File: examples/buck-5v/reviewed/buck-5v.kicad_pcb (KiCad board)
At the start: 2 copper layers, 126 x 56 mm, 11 parts, among them J1 12V IN, J2 5V OUT, U1 LM2596S-5

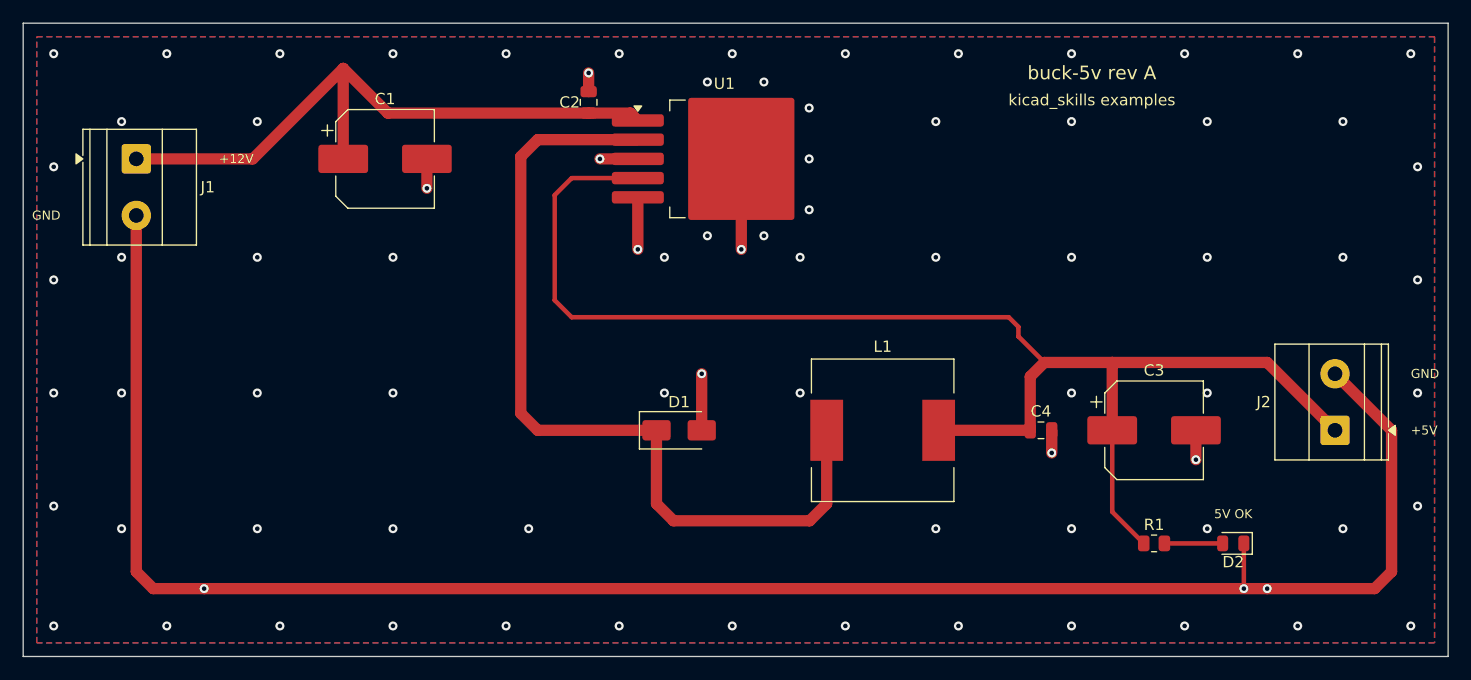
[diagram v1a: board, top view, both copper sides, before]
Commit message: Relieve the pads, fillet the joints, and give the board its screw holes
Three of the reviewer's manufacturing points, and they largely fall out
of the one before it - once KiCad fills the plane, the thermal relief it
was already asked for in the file actually appears.

**Thermal relief.** The zones said thermal all along; our own filler
ignored it and flooded every land solid. KiCad's does not, so every
through-hole ground pad now sits in a gap bridged by four spokes and an
iron can bring the joint up without heating a hundred square millimetres
of copper. `layout.solid_pad_connection` reports the setting when a
board turns it off: drilled pads only, because a surface pad reflows in
an oven that is heating the plane anyway and flooding it is often the
better thermal answer.

**Teardrops.** A track entering a land is a step change in width, and a
step change is where copper tears - the connector gets levered on and
off, the drill wanders, and the crack starts at the corner. `_teardrops`
replaces the first stretch of each run with a three-step taper into the
land, checked against its neighbours before it is kept, so a fillet
never eats the clearance a fine-pitch escape needs. It *replaces* rather
than overlays: laying the taper on top of the run drew the same copper
twice, and `route.acute_angle` reported all thirty of them, correctly.
`route.mixed_track_widths` learns what a fillet looks like so a properly
filleted board does not read as one nobody decided the width of.

**Mounting holes.** Four M3 holes near the corners, placed before the
router runs because they are obstacles, and slid along the edges or a
little inboard where a connector body has the corner - the motor board
and the op-amp take three, which is what those floorplans have room for.
Grounded on the motor driver, whose chassis is metal and part of the
shield, plain on the rest: bonding the enclosure to the reference is the
enclosure's decision, not the board's.

Two things that fell out of placing par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
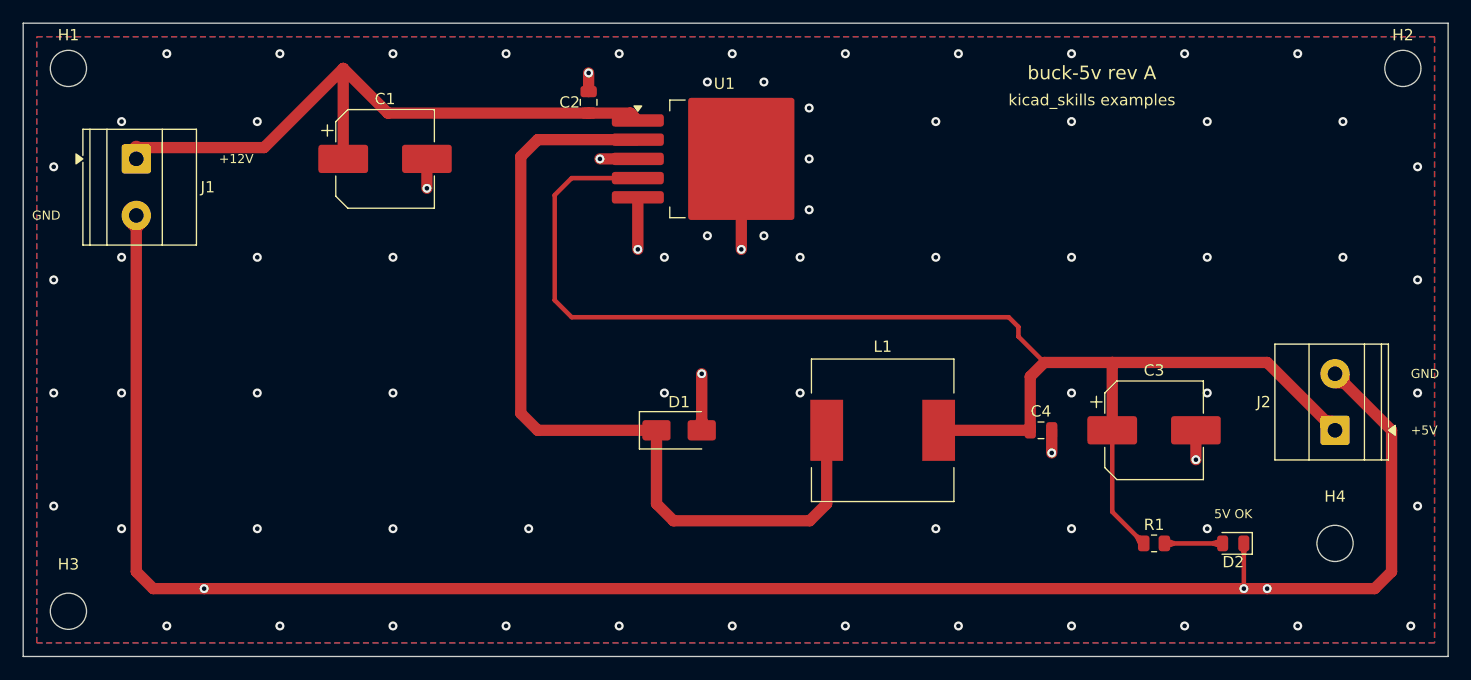
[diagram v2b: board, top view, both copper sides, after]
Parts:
- added H1: M33, MountingHole:MountingHole_3.2mm_M3, F.Cu at (104.0, 64.0)
- added H2: M33, MountingHole:MountingHole_3.2mm_M3, F.Cu at (222.0, 64.0)
- added H3: M33, MountingHole:MountingHole_3.2mm_M3, F.Cu at (104.0, 112.0)
- added H4: M33, MountingHole:MountingHole_3.2mm_M3, F.Cu at (216.0, 106.0)
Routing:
- net /+12V: track 57.6 -> 58.2 mm
- net GND: vias 82 -> 78

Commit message: Give the assembly machine something to aim at
Fiducials: three copper dots in bare mask windows, near three different
corners so a pick-and-place gets rotation as well as offset. It aligns
to the board, not to the drawing - without them it has only the routed
outline, cut to a tolerance ten times looser than the placement a 0.5 mm
pitch part is asking for. `fab.no_fiducials` reports a fine-pitch board
that has none, as context rather than as a fault: plenty of boards are
built one at a time with tweezers.

They share the corner search with the mounting holes, which is where
this found a real bug: `_courtyard_box` read lines and rectangles only,
and a mounting hole draws its courtyard as one circle - so every hole
measured as taking up no room at all, and the first three fiducials
landed on top of three screw holes. Circles and arcs count now.

Co-Authored-By: Claude Fable 5 <noreply@anthropic.com>
Claude-Session: https://claude.ai/code/session_01DUj7Ltu92tWg159mCSacwY
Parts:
- added FID1: Fiducial, Fiducial:Fiducial_1mm_Mask2mm, F.Cu at (102.5, 69.5)
- added FID2: Fiducial, Fiducial:Fiducial_1mm_Mask2mm, F.Cu at (216.5, 62.5)
- added FID3: Fiducial, Fiducial:Fiducial_1mm_Mask2mm, F.Cu at (109.5, 113.5)
- H1, H2, H3, H4: value M33 -> M3

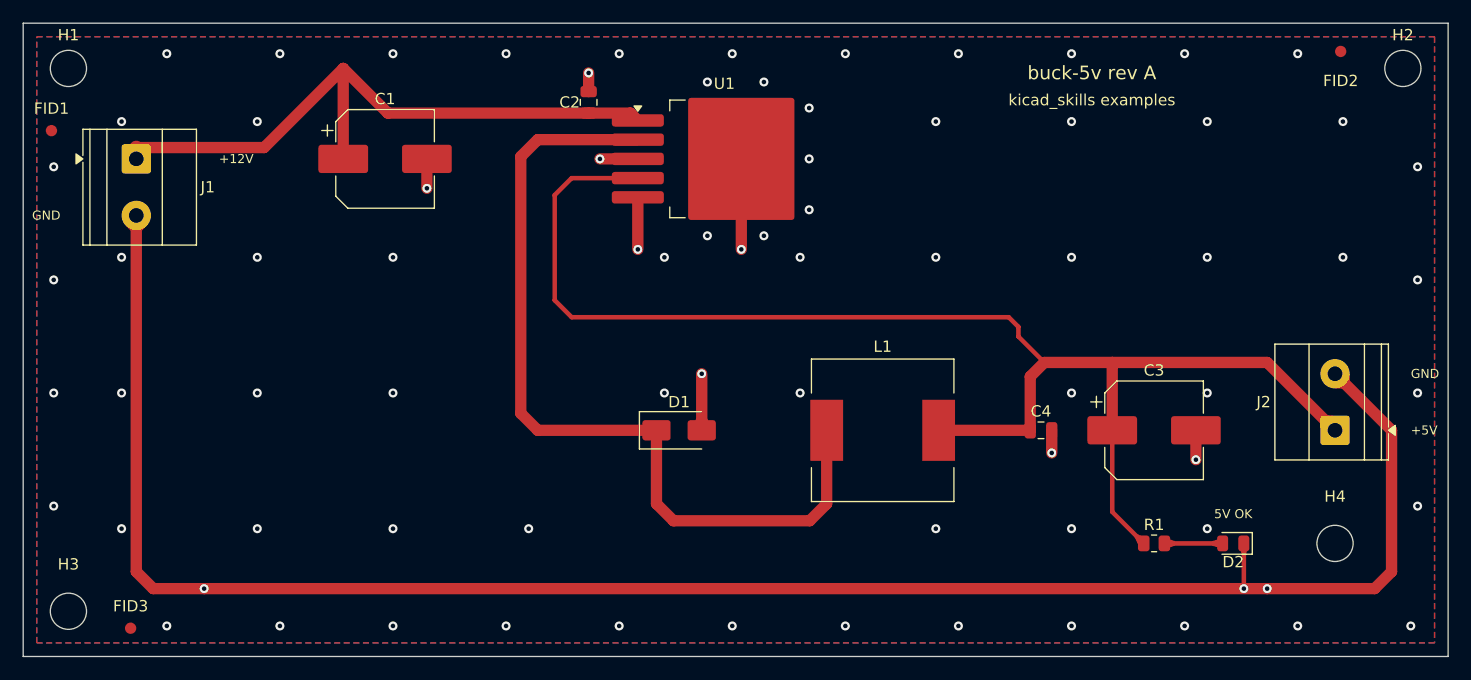
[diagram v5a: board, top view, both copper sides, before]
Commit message: Leave room for the screw, and print the ink where the board is
The screw holes were placed against the hole's own courtyard, which is the
drill plus a whisker - so on four of the five boards a hole sat inside a
connector's mating space, closest 0.42 mm. What goes through an M3 hole is a
pan head on a washer, seven millimetres of steel lying flat, and a connector
wants its shell, its wires and the fingers that fit them on top of that. The
spot search now keeps the fastener's own circle clear of every part body and
gives connectors CONNECTOR_ACCESS more, and three rules say so when a board
does not: mechanical.fastener_clearance, mechanical.connector_access and
mechanical.fastener_copper, all blocking for a generated design.

Silk was measured with a per-character advance of 0.78, and KiCad's stroke
font is proportional at 0.94 to 1.07. Everything downstream of that estimate
was placing ink where it did not fit: a legend across a capacitor's land, a
designator through the board's own name. `_text_extent` takes the top of the
measured range, adds the fab's clearance and is used by every silk placement.

Three placements also fell through to a position nobody chose. A designator
that found nothing kept its library offset, which for a part in a corner
points off the board; the board id took the first of eight fixed strips; a
legend took the least bad of six spots. All three are scored now, over
candidate sets wide enough to have an answer - and a pad-less footprint, which
is what a mounting hole is, is no longer skipped outright.

silk.off_board reports the case KiCad's own test cannot: ink that clears the
edge entirely is never printed, and DRC only measures ink that crosses it.

_unspiked redraws a corner tighter than a right angle as the elbow between its
neighbours - one diagonal, one straight, no step back to a heading the line
has already left. It is never longer than what it replaces.

All four fast boards: 0 errors, 0 warnings.

Co-Authored-By: Claude Fable 5 <no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
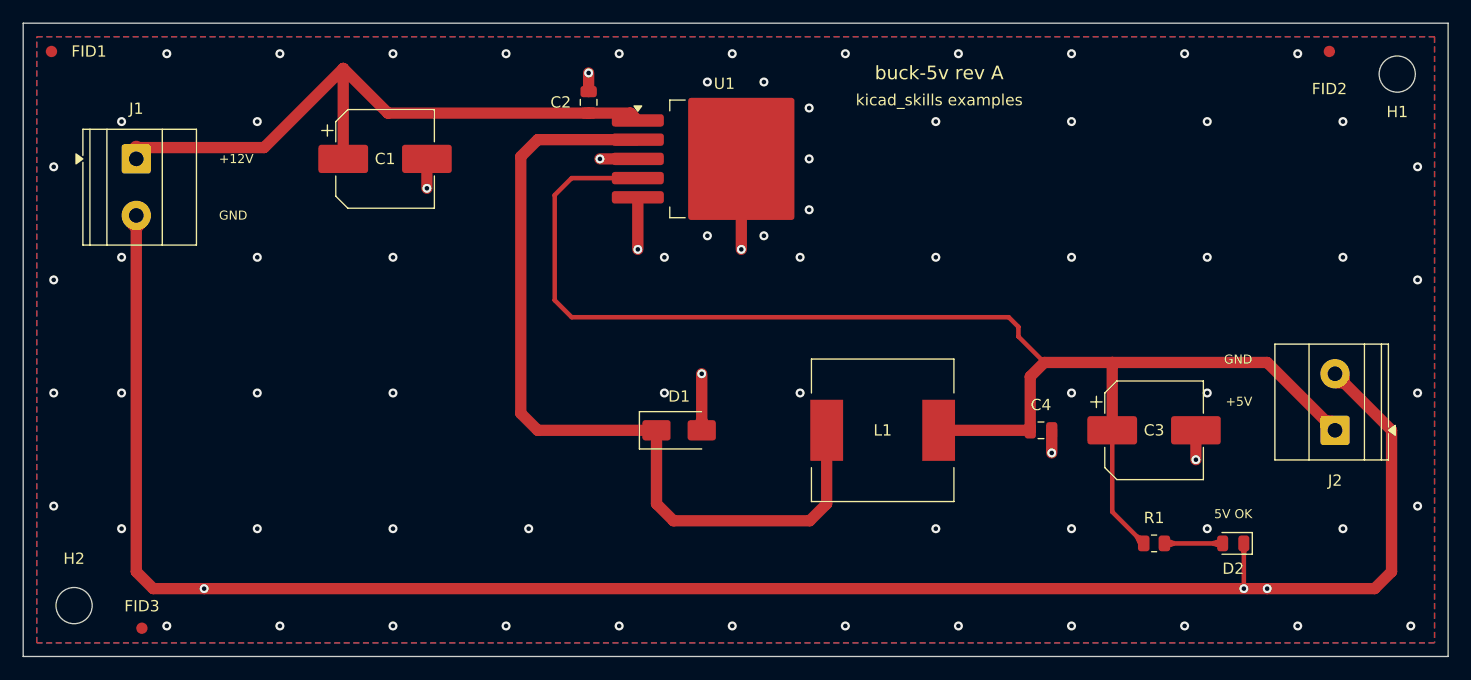
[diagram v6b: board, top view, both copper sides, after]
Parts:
- removed H3, H4: M3, MountingHole:MountingHole_3.2mm_M3
- moved H2 126.7 mm to (104.5, 111.5)
- moved H1 117.5 mm to (221.5, 64.5)
- moved FID1 7.00 mm to (102.5, 62.5)
- moved FID2 1.00 mm to (215.5, 62.5)
- moved FID3 1.00 mm to (110.5, 113.5)
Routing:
- net GND: vias 78 -> 79

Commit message: Walk the whole edge for a screw hole, and land a joint on its own pad
The fastener clearance was right and the search was not: it slid along two
edges from each corner and gave up, so boards that had had four screw holes
came back with one. It now walks a ring round the board at the inset the
screw needs, taking the nearest free point to each corner - and only from
that corner's own quarter, because a search that asked for the nearest free
point anywhere put three of the four along one edge, each of them the nearest
thing to a different corner. A quarter with no room gives no screw: three
that hold the board flat beat four that hold one side.

A pin header asks for nothing above its courtyard - the socket that fits it
lands inside the outline the header already draws - while a screw terminal's
wires leave horizontally from its face. Treating the two alike is what left a
carrier lined with headers with two holes on one edge. Both the generator and
the rule now tell them apart by footprint.

_landed folds a via that sits beside a plated hole of its own net onto the
hole. The plating already joins the faces, so the via bought nothing and cost
hole-to-hole: two drills a millimetre apart leave 0.15 mm of laminate at a
0.25 mm rule, which is what DRC reported on the opamp board.

The fillets move to the end of the pipeline. A taper is built against the end
of a run, and _landed moves ends, so a teardrop laid before it pointed at
where the run used to stop - a nought-degree corner in the angle rule.

buck-5v, motor-driver, pico-carrier, opamp-filter: 0 errors, 0 warnings.

Co-Authored-By: Claude Fable 5 <noreply@anthropic.com>
Claude-Session: https://claude.ai/code/session_01DUj7Ltu92tWg159mCSacwY
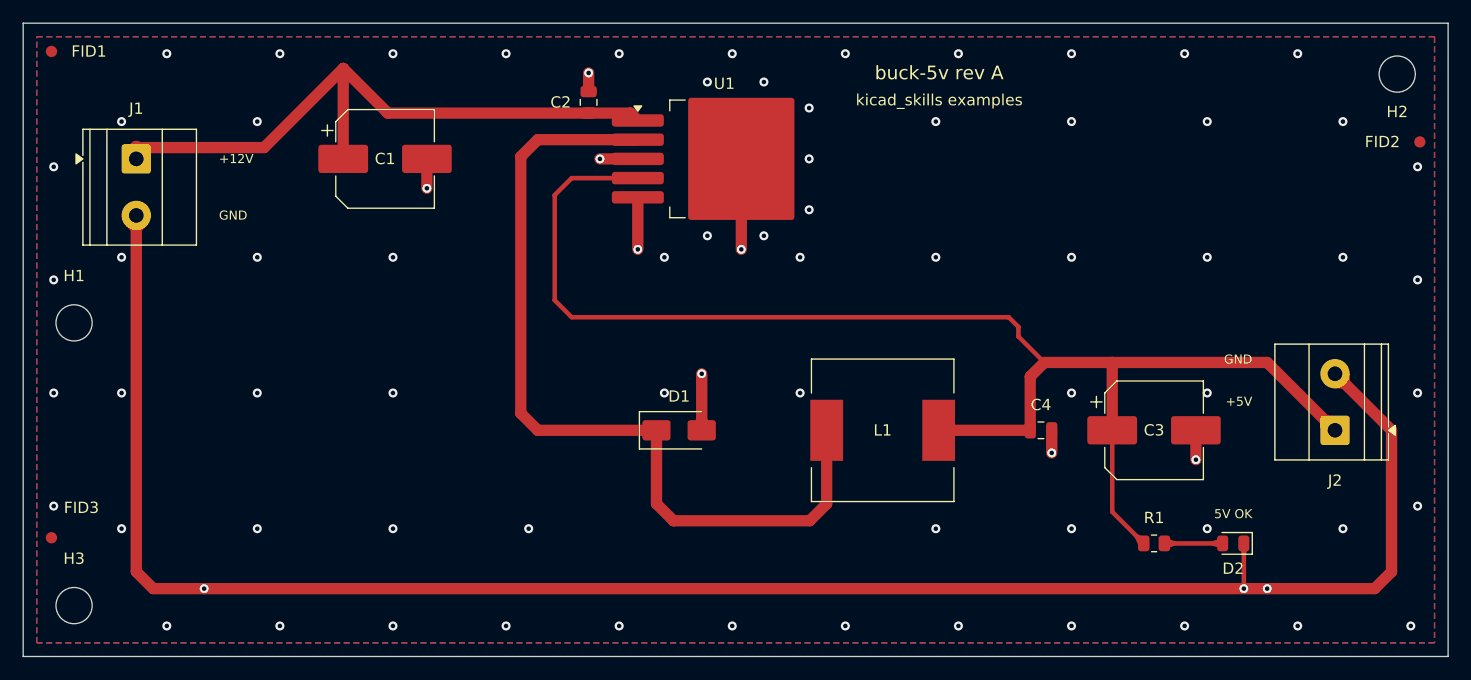
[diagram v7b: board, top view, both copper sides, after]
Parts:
- added H3: M3, MountingHole:MountingHole_3.2mm_M3, F.Cu at (104.5, 111.5)
- moved H2 126.1 mm to (221.5, 64.5)
- moved H1 119.1 mm to (104.5, 86.5)
- moved FID2 11.3 mm to (223.5, 70.5)
- moved FID3 11.3 mm to (102.5, 105.5)
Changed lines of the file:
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@@
 	(footprint "MountingHole:MountingHole_3.2mm_M3"
 		(layer "F.Cu")
-		(at 104.5 111.5)
+		(at 221.5 64.5)
 		(descr "Mounting Hole 3.2mm, M3, no annular, generated by kicad-footprint-generator mountinghole.py")
 		(tags "mountinghole M3")
 		(property "Reference" "H2"
-			(at 0 -4.15 0)
+			(at 0 3.345 0)
 			(layer "F.SilkS")
 			(effects
@@
 		)
 		(property "MPN" "n/a"
-			(at 0 -4.15 0)
+			(at 0 3.345 0)
 			(layer "F.Fab")
 			(hide yes)
@@
 		)
 		(property "Manufacturer" "n/a"
-			(at 0 -4.15 0)
+			(at 0 3.345 0)
 			(layer "F.Fab")
 			(hide yes)
@@
 	(footprint "Fiducial:Fiducial_1mm_Mask2mm"
 		(layer "F.Cu")
-		(at 215.5 62.5)
+		(at 223.5 70.5)
 		(descr "Fiducial, circular marking, 1mm bare copper, 2mm soldermask opening (Level A)")
 		(tags "fiducial")
 		(property "Reference" "FID2"
-			(at 0 3.315 0)
+			(at -3.315 0 0)
 			(layer "F.SilkS")
 			(effects
@@
 		)
 		(property "MPN" "n/a"
-			(at 0 3.315 0)
+			(at -3.315 0 0)
 			(layer "F.Fab")
 			(hide yes)
@@
 		)
 		(property "Manufacturer" "n/a"
-			(at 0 3.315 0)
+			(at -3.315 0 0)
 			(layer "F.Fab")
 			(hide yes)
@@
 		)
 	)
+	(footprint "MountingHole:MountingHole_3.2mm_M3"
+		(layer "F.Cu")
+		(at 104.5 111.5)
+		(descr "Mounting Hole 3.2mm, M3, no annular, generated by kicad-footprint-generator mountinghole.py")
+		(tags "mountinghole M3")
+		(property "Reference" "H3"
+			(at 0 -4.15 0)
+			(layer "F.SilkS")
+			(effects
+				(font
+					(size 1 1)
+					(thickness 0.15)
+				)
+			)
+		)
+		(property "Value" "M3"
+			(at 0 4.15 0)
+			(layer "F.Fab")
+			(effects
+				(font
+					(size 1 1)
+					(thickness 0.15)
+				)
+			)
+		)
+		(property "Datasheet" ""
+			(at 0 0 0)
+			(layer "F.Fab")
+			(hide yes)
+			(effects
+				(font
+					(size 1.27 1.27)
+					(thickness 0.15)
+				)
+			)
+		)
+		(property "Description" ""
+			(at 0 0 0)
+			(layer "F.Fab")
+			(hide yes)
+			(effects
+				(font
+					(size 1.27 1.27)
+					(thickness 0.15)
+				)
+			)
+		)
+		(property "MPN" "n/a"
+			(at 0 -4.15 0)
+			(layer "F.Fab")
+			(hide yes)
+			(effects
+				(font
+					(size 1 1)
+					(thickness 0.15)
+				)
+			)
+		)
+		(property "Manufacturer" "n/a"
+			(at 0 -4.15 0)
+			(layer "F.Fab")
+			(hide yes)
+			(effects
+				(font
+					(size 1 1)
+					(thickness 0.15)
+				)
+			)
+		)
+		(attr exclude_from_pos_files exclude_from_bom)
+		(fp_circle
+			(center 0 0)
+			(end 3.2 0)
+			(stroke
+				(width 0.15)
+				(type solid)
+			)
+			(fill no)
+			(layer "Cmts.User")
+		)
+		(fp_circle
+			(center 0 0)
+			(end 3.45 0)
+			(stroke
+				(width 0.05)
+				(type solid)
+			)
+			(fill no)
+			(layer "F.CrtYd")
+		)
+		(fp_text user "${REFERENCE}"
+			(at 0 0 0)
+			(layer "F.Fab")
+			(effects
+				(font
+					(size 1 1)
+					(thickness 0.15)
+				)
+			)
+		)
+		(pad "" np_thru_hole circle
+			(at 0 0)
+			(size 3.2 3.2)
+			(drill 3.2)
+			(layers "*.Cu" "*.Mask")
+		)
+		(embedded_fonts no)
+	)
 	(footprint "Capacitor_SMD:C_0805_2012Metric"
 		(layer "F.Cu")
@@
 	(footprint "Fiducial:Fiducial_1mm_Mask2mm"
 		(layer "F.Cu")
-		(at 110.5 113.5)
+		(at 102.5 105.5)
 		(descr "Fiducial, circular marking, 1mm bare copper, 2mm soldermask opening (Level A)")
 		(tags "fiducial")
 		(property "Reference" "FID3"
-			(at 0 -1.95 0)
+			(at 2.652 -2.652 0)
 			(layer "F.SilkS")
 			(effects
@@
 		)
 		(property "MPN" "n/a"
-			(at 0 -1.95 0)
+			(at 2.652 -2.652 0)
 			(layer "F.Fab")
 			(hide yes)
@@
 		)
 		(property "Manufacturer" "n/a"
-			(at 0 -1.95 0)
+			(at 2.652 -2.652 0)
 			(layer "F.Fab")
 			(hide yes)
@@
 	(footprint "MountingHole:MountingHole_3.2mm_M3"
 		(layer "F.Cu")
-		(at 221.5 64.5)
+		(at 104.5 86.5)
 		(descr "Mounting Hole 3.2mm, M3, no annular, generated by kicad-footprint-generator mountinghole.py")
 		(tags "mountinghole M3")
 		(property "Reference" "H1"
-			(at 0 3.345 0)
+			(at 0 -4.15 0)
 			(layer "F.SilkS")
 			(effects
@@
 		)
 		(property "MPN" "n/a"
-			(at 0 3.345 0)
+			(at 0 -4.15 0)
 			(layer "F.Fab")
 			(hide yes)
@@
 		)
 		(property "Manufacturer" "n/a"
-			(at 0 3.345 0)
+			(at 0 -4.15 0)
 			(layer "F.Fab")
 			(hide yes)
